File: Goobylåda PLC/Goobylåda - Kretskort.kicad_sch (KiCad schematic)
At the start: 99 parts, among them J1 LCD 1602 kontakt, J10 Anslutning, J11 Anslutning, J12 Anslutning, J13 Anslutning, J14 Anslutning, J15 Anslutning, J16 Anslutning, J17 Anslutning, J18 Anslutning, J2 Anslutning, J3 Anslutning, J4 Anslutning, J5 Anslutning, J6 Anslutning, J7 Anslutning, J8 Anslutning, J9 Anslutning, Q1 2N2222, Q10 MJE2955T, Q11 MJE2955T, Q12 MJE2955T, Q2 2N2222, Q3 2N2222, Q4 IRF9630, Q5 IRF9630, Q6 IRF9630, Q7 2N2222, Q8 2N2222, Q9 2N2222, U1 LM7812_TO220

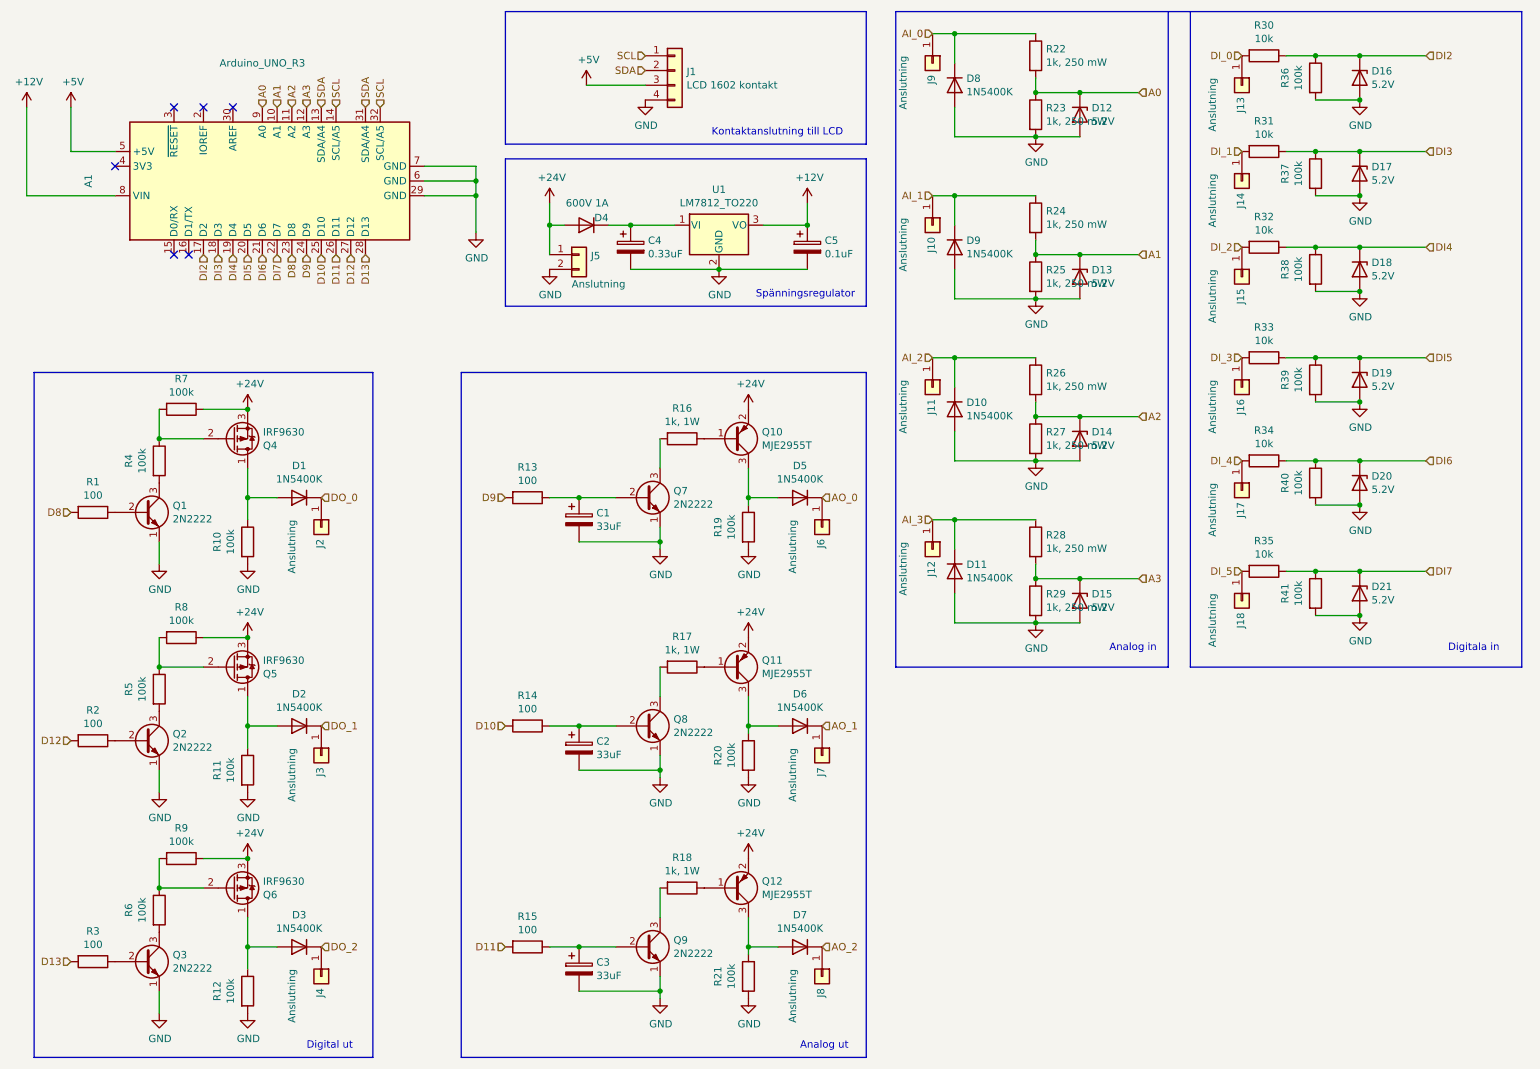
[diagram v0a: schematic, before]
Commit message: Update for THT
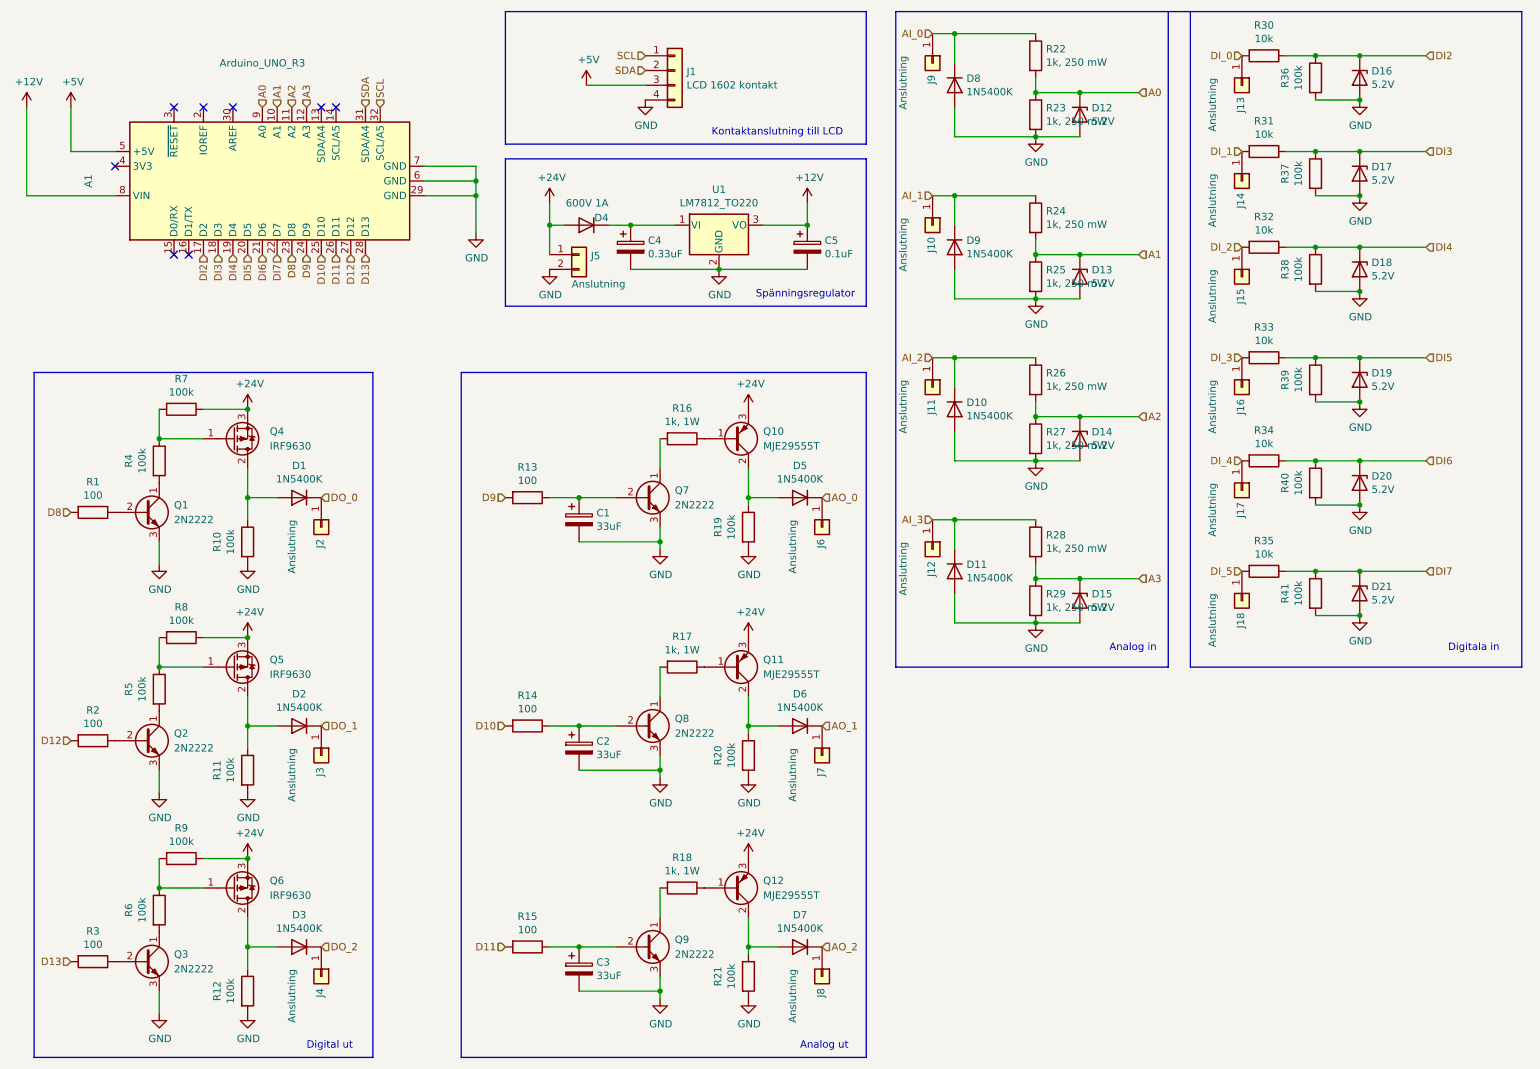
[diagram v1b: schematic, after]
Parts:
- removed Q1, Q2, Q3, Q7, Q8, Q9: 2N2222, Package_TO_SOT_THT:TO-92, symbol Transistor_BJT:2N2219
- removed Q10, Q11, Q12: MJE2955T, Package_TO_SOT_THT:TO-220-3_Vertical, symbol Transistor_BJT:MJ2955
- removed Q4, Q5, Q6: IRF9630, Package_TO_SOT_THT:TO-220-3_Vertical, symbol Transistor_FET:IRF9383M
- added Q1, Q2, Q3, Q7, Q8, Q9: 2N2222, Package_TO_SOT_THT:TO-92_Inline, symbol Transistor_BJT:BC547
- added Q10, Q11, Q12: MJE29555T, Package_TO_SOT_THT:TO-220-3_Vertical, symbol Device:Q_PNP_BCE
- added Q4, Q5, Q6: IRF9630, Package_TO_SOT_THT:TO-220-3_Vertical, symbol Transistor_FET:IRF9540N
- D1, D10, D11, D2, D3, D5, D6, D7, D8, D9: footprint Diode_THT:D_DO-15_P10.16mm_Horizontal -> Diode_THT:D_DO-15_P12.70mm_Horizontal
- D4: footprint Diode_THT:D_DO-41_SOD81_P7.62mm_Horizontal -> Diode_THT:D_DO-41_SOD81_P10.16mm_Horizontal
- R1, R10, R11, R12, R13, R14, R15, R19, R2, R20, R21, R3, R30, R31, R32, R33, R34, R35, R36, R37, R38, R39, R4, R40, R41, R5, R6, R7, R8, R9: footprint Resistor_THT:R_Axial_DIN0204_L3.6mm_D1.6mm_P5.08mm_Horizontal -> Resistor_THT:R_Axial_DIN0204_L3.6mm_D1.6mm_P7.62mm_Horizontal
- R22, R23, R24, R25, R26, R27, R28, R29: footprint Resistor_THT:R_Axial_DIN0204_L3.6mm_D1.6mm_P5.08mm_Horizontal -> Resistor_THT:R_Axial_DIN0207_L6.3mm_D2.5mm_P10.16mm_Horizontal
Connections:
- net +24V: now also Q10.3 (E), Q11.3 (E), Q12.3 (E), Q4.3 (S), Q5.3 (S), Q6.3 (S)
- net GND: now also Q1.3 (E), Q2.3 (E), Q3.3 (E), Q7.3 (E), Q8.3 (E), Q9.3 (E)
- net SCL: no longer A1.14 (SCL/A5)
- net SDA: no longer A1.13 (SDA/A4)
- net at R1.1: now also Q1.2 (B)
- net at R4.2: now also Q1.1 (C)
- net at R4.1, R7.2: now also Q4.1 (G)
- net at R16.1: now also Q10.1 (B)
- net at D5.2 (A), R19.1: now also Q10.2 (C)
- net at C1.1, R13.1: now also Q7.2 (B)
- net at R16.2: now also Q7.1 (C)
- net at D2.2 (A), R11.1: now also Q5.2 (D)
- net at R5.1, R8.2: now also Q5.1 (G)
- net at R2.1: now also Q2.2 (B)
- net at R5.2: now also Q2.1 (C)
- net at R17.1: now also Q11.1 (B)
- net at D6.2 (A), R20.1: now also Q11.2 (C)
- net at C2.1, R14.1: now also Q8.2 (B)
- net at R17.2: now also Q8.1 (C)
- net at R18.1: now also Q12.1 (B)
- net at D7.2 (A), R21.1: now also Q12.2 (C)
- net at C3.1, R15.1: now also Q9.2 (B)
- net at R18.2: now also Q9.1 (C)
- net at D3.2 (A), R12.1: now also Q6.2 (D)
- net at R6.1, R9.2: now also Q6.1 (G)
- net at R3.1: now also Q3.2 (B)
- net at R6.2: now also Q3.1 (C)
- net at D1.2 (A), R10.1: now also Q4.2 (D)
- no-connect marks 6 -> 8
